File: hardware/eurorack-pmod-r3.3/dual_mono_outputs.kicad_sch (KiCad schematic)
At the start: 20 parts, among them J8 AUDIO JACK PJ-324M0, J9 AUDIO JACK PJ-324M0, Q2 MMBFJ111, Q4 MMBFJ111, U2 TL074 OP AMP

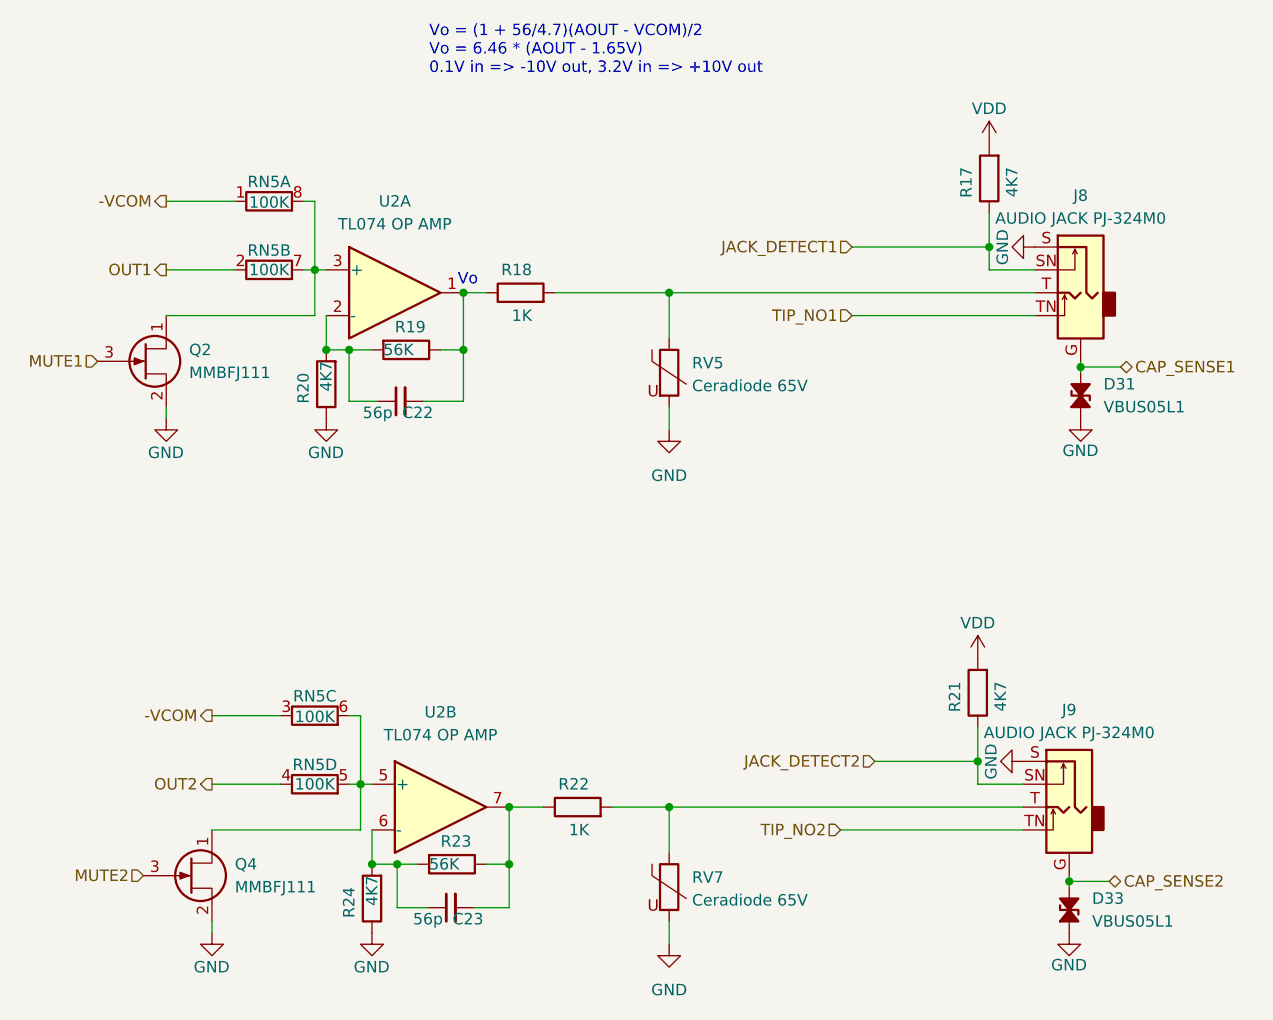
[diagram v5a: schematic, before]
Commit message: r3.5: add 100k output terminations and 100nF vref filtering, fab outputs (not sent yet)
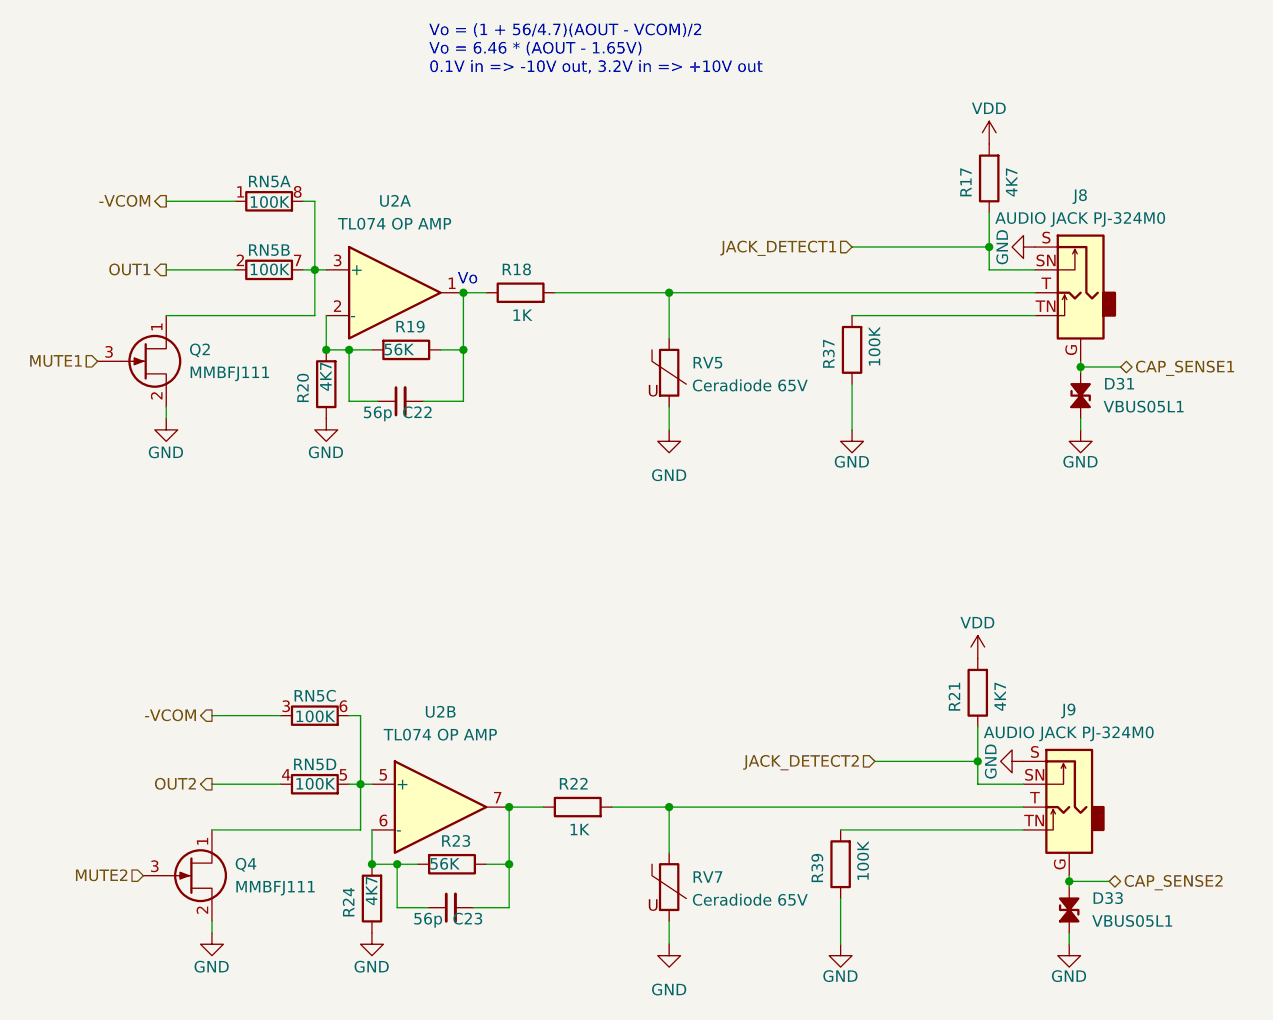
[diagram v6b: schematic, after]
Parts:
- added R37, R39: 100K, Resistor_SMD:R_0603_1608Metric, symbol Device:R
- Q2, Q4: LCSC (none) -> C274688
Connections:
- net GND: now also R37.1, R39.1
- net TIP_NO1: no longer names the net of J8.TN
- net TIP_NO1: now also R37.2
- net TIP_NO2: no longer names the net of J9.TN
- net TIP_NO2: now also R39.2
